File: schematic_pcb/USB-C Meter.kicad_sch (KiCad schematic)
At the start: 53 parts, among them J1 USB_B_Micro, J2 USB-C Receptacle 6P, J3 Generic IN, J4 Generic OUT, J5 USB-C Receptacle 6P, J6 Conn_Coaxial, J7 UART, U1 XL1509-3.3, U2 ME6211C33, U3 TPS2115, U4 ESP32-C3FH4, U6 INA228, U7 Display I2C, Y1 40MHz

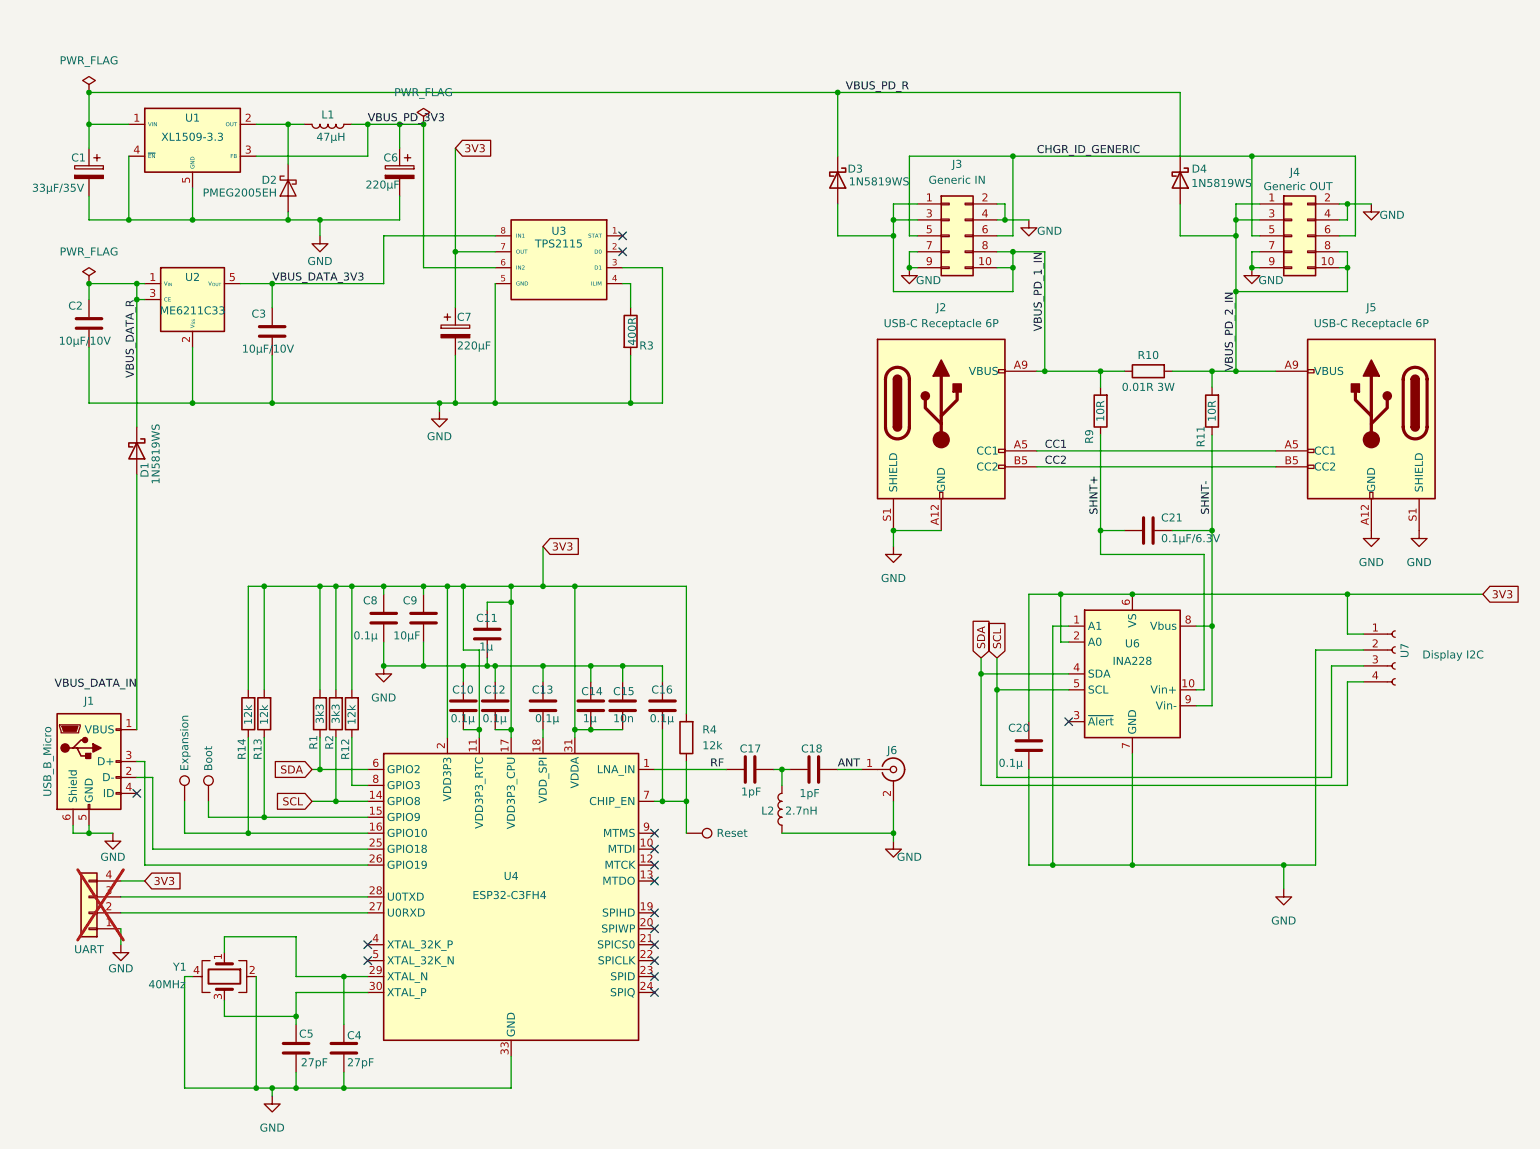
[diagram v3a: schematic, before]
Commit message: feat(hw): new buck converter enables up to 48V PD input
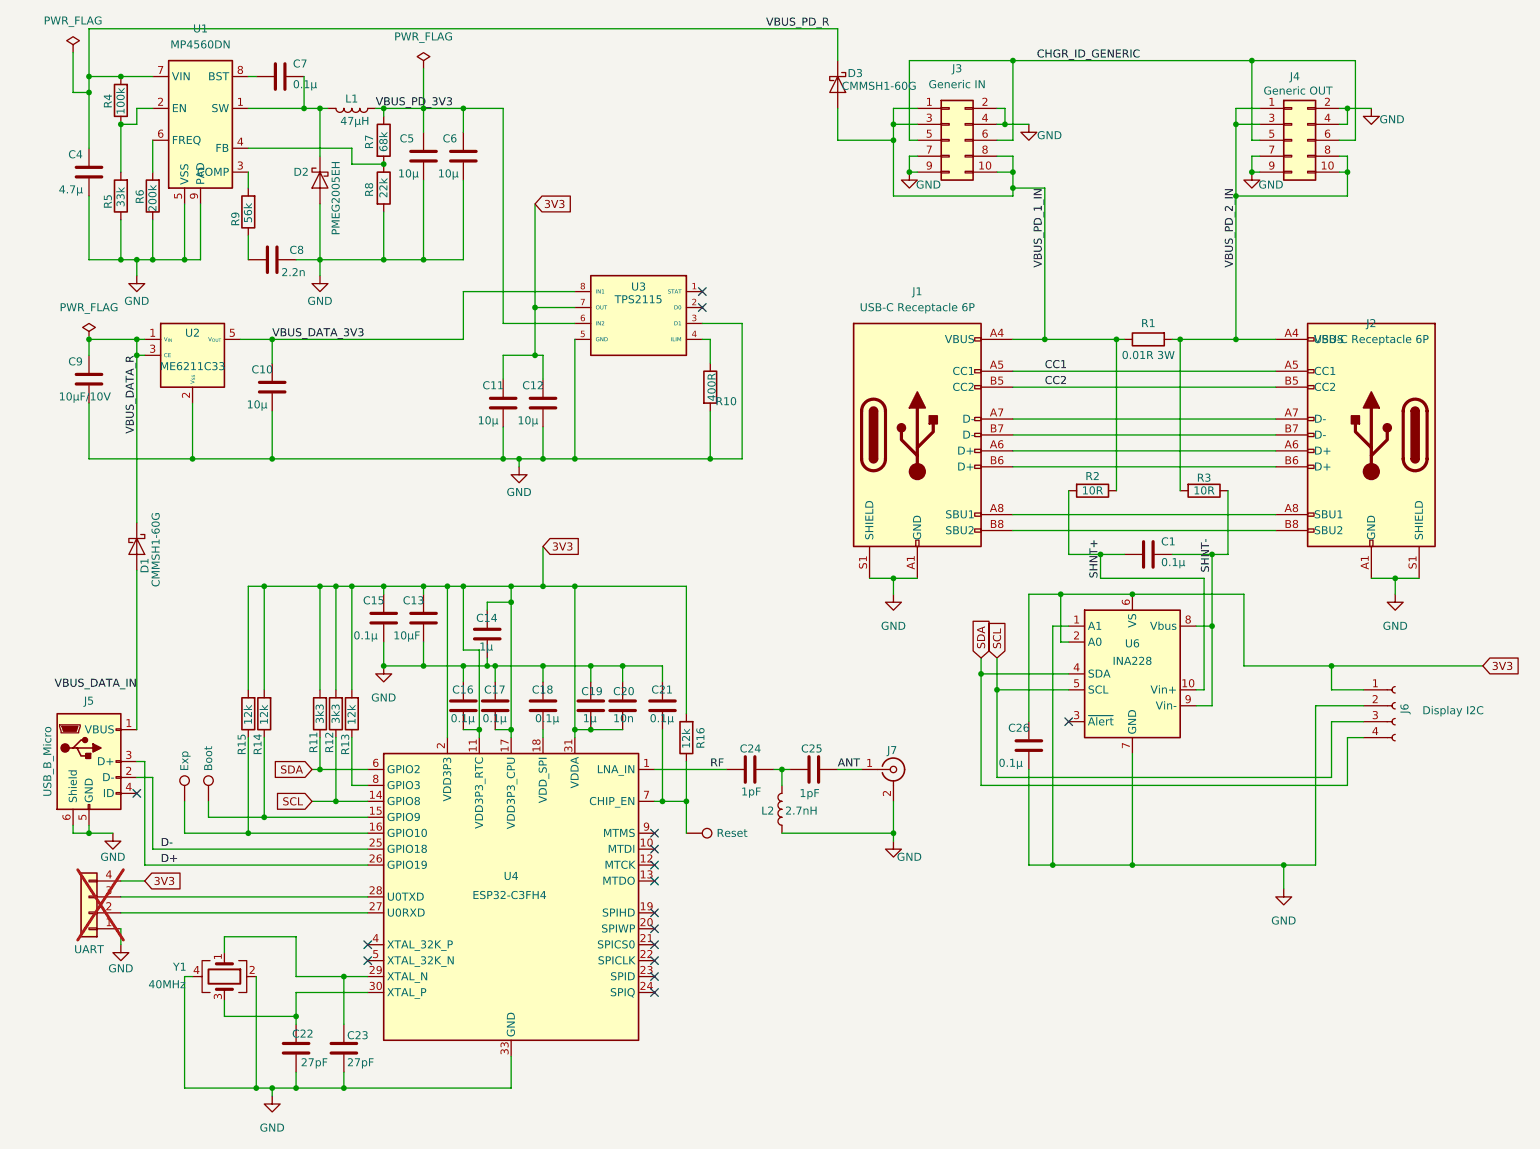
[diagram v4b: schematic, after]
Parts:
- removed C1: 33µF/35V, Capacitor_SMD:CP_Elec_5x5.8, symbol Device:C_Polarized
- removed C6, C7: 220µF, Capacitor_SMD:CP_Elec_6.3x5.9, symbol Device:C_Polarized
- removed D4: 1N5819WS, Diode_SMD:D_SOD-123F, symbol Diode:1N5819WS
- removed U1: XL1509-3.3, Package_SO:SOIC-8_3.9x4.9mm_P1.27mm, symbol Regulator_Switching:XL1509-3.3
- added C11, C12, C5, C6: 10µ, Capacitor_SMD:C_0603_1608Metric, symbol Device:C
- added C4: 4.7µ, Capacitor_SMD:C_0805_2012Metric_Pad1.18x1.45mm_HandSolder, symbol Device:C
- added C7: 0.1µ, Capacitor_SMD:C_0603_1608Metric, symbol Device:C
- added C8: 2.2n, Capacitor_SMD:C_0603_1608Metric, symbol Device:C
- added R4: 100k, Resistor_SMD:R_0603_1608Metric_Pad0.98x0.95mm_HandSolder, symbol Device:R
- added R5: 33k, Resistor_SMD:R_0603_1608Metric_Pad0.98x0.95mm_HandSolder, symbol Device:R
- added R6: 200k, Resistor_SMD:R_0603_1608Metric_Pad0.98x0.95mm_HandSolder, symbol Device:R
- added R7: 68k, Resistor_SMD:R_0603_1608Metric_Pad0.98x0.95mm_HandSolder, symbol Device:R
- added R8: 22k, Resistor_SMD:R_0603_1608Metric_Pad0.98x0.95mm_HandSolder, symbol Device:R
- added R9: 56k, Resistor_SMD:R_0603_1608Metric_Pad0.98x0.95mm_HandSolder, symbol Device:R
- added U1: MP4560DN, Package_SO:SOIC-8_3.9x4.9mm_P1.27mm, symbol Driver_FET:MP4560
- C1: renamed from C21; value 0.1µF/6.3V -> 0.1µ; Link (none) -> https://www.mouser.de/ProductDetail/YAGEO/CC0603MRY5V9BB104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; Price (none) -> 0,018
- C10: renamed from C3; value 10µF/10V -> 10µ; Link (none) -> https://www.mouser.de/ProductDetail/Samsung-Electro-Mechani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; Price (none) -> 0,20
- C13: renamed from C9; Link (none) -> https://www.mouser.de/ProductDetail/KYOCERA-AVX/06036D106MA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; Price (none) -> 0,058
- C14: renamed from C11; Link (none) -> https://www.mouser.de/ProductDetail/YAGEO/CC0603KRX5R8BB105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; Price (none) -> 0,034
- C15: renamed from C8; Link (none) -> https://www.mouser.de/ProductDetail/YAGEO/CC0603MRY5V9BB104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; Price (none) -> 0,018
- C16: renamed from C10; Link (none) -> https://www.mouser.de/ProductDetail/YAGEO/CC0603MRY5V9BB104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; Price (none) -> 0,018
- C17: renamed from C12; Link (none) -> https://www.mouser.de/ProductDetail/YAGEO/CC0603MRY5V9BB104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; Price (none) -> 0,018
- C18: renamed from C13; Link (none) -> https://www.mouser.de/ProductDetail/YAGEO/CC0603MRY5V9BB104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; Price (none) -> 0,018
- C19: renamed from C14; Link (none) -> https://www.mouser.de/ProductDetail/YAGEO/CC0603KRX5R8BB105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; Price (none) -> 0,034
- C20: renamed from C15; Link (none) -> https://www.mouser.de/ProductDetail/KYOCERA-AVX/06035C103K4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; Price (none) -> 0,074
- C21: renamed from C16; Link (none) -> https://www.mouser.de/ProductDetail/YAGEO/CC0603MRY5V9BB104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; Price (none) -> 0,018
- C22: renamed from C5; Link (none) -> https://www.mouser.de/ProductDetail/KYOCERA-AVX/04025A270JA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; Price (none) -> 0,016
- C23: renamed from C4; Link (none) -> https://www.mouser.de/ProductDetail/KYOCERA-AVX/04025A270JA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; Price (none) -> 0,016
- C24: renamed from C17; Link (none) -> https://www.mouser.de/ProductDetail/KYOCERA-AVX/04023A1R0BA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; Price (none) -> 0,163
- C25: renamed from C18; Link (none) -> https://www.mouser.de/ProductDetail/KYOCERA-AVX/04023A1R0BA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; Price (none) -> 0,163
- C26: renamed from C20; Link (none) -> https://www.mouser.de/ProductDetail/YAGEO/CC0603MRY5V9BB104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; Price (none) -> 0,018
- C9: renamed from C2; Link (none) -> https://www.mouser.de/ProductDetail/Samsung-Electro-Mechani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; Price (none) -> 0,20
- D1, D3: value 1N5819WS -> CMMSH1-60G; footprint Diode_SMD:D_SOD-123F -> Diode_SMD:Nexperia_CFP3_SOD-123W; symbol Diode:1N5819WS -> Diode:PMEG60T10ELR; Price (none) -> 0,218; url (none) -> https://www.mouser.de/ProductDetail/Nexperia/PMEG6010CEGW-Q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
- D2: Price (none) -> 0,092; url (none) -> https://www.mouser.de/ProductDetail/Nexperia/PMEG2005EH115?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
- J1: renamed from J2; footprint Connector_USB:USB_C_Receptacle_GCT_USB4125-xx-x_6P_TopMnt_Horizontal -> Connector_USB:USB_C_Receptacle_XKB_U262-16XN-4BVC11; symbol Connector:USB_C_Receptacle_PowerOnly_6P -> Connector:USB_C_Receptacle_USB2.0_16P
- J2: renamed from J5; footprint Connector_USB:USB_C_Receptacle_HRO_TYPE-C-31-M-17 -> Connector_USB:USB_C_Receptacle_XKB_U262-16XN-4BVC11; symbol Connector:USB_C_Receptacle_PowerOnly_6P -> Connector:USB_C_Receptacle_USB2.0_16P
- J3: Price (none) -> 0,791; url (none) -> https://www.mouser.de/ProductDetail/TE-Connectivity/826634-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
- J4: Price (none) -> 1,44; url (none) -> https://www.mouser.de/ProductDetail/Samtec/SSQ-105-02-T-D-R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
- J5: renamed from J1; Price (none) -> 1,74; url (none) -> https://www.mouser.de/ProductDetail/Wurth-Elektronik/629105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
- J6: renamed from U7; Price (none) -> 2,50; url (none) -> https://de.aliexpress.com/item/1005007759329196.html?spm=a2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
- J7: renamed from J6; Price (none) -> 1,12; url (none) -> https://www.mouser.de/ProductDetail/Hirose-Connector/U.FL-R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
- L1: Price (none) -> 1,05; url (none) -> https://www.mouser.de/ProductDetail/TE-Connectivity-Sigma-I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
- L2: Price (none) -> 0,123; url (none) -> https://www.mouser.de/ProductDetail/TE-Connectivity-Sigma-I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
- R1: renamed from R10; Price (none) -> 0,586; url (none) -> https://www.mouser.de/ProductDetail/Vishay-Dale/WSLP2512R01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
- R10: renamed from R3; Price (none) -> 0,086; url (none) -> https://www.mouser.de/ProductDetail/Vishay-Beyschlag/MCS040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
- R11: renamed from R1; Price (none) -> 0,086; url (none) -> https://www.mouser.de/ProductDetail/Bourns/CR0603-JW-332ELF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
- R12: renamed from R2; Price (none) -> 0,086; url (none) -> https://www.mouser.de/ProductDetail/Bourns/CR0603-JW-332ELF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
- R13: renamed from R12; Price (none) -> 0,086
- R14: renamed from R13; Price (none) -> 0,086
- R15: renamed from R14; Price (none) -> 0,086
- R16: renamed from R4; Price (none) -> 0,086
- R2: renamed from R9; Price (none) -> 0,086
- R3: renamed from R11; Price (none) -> 0,086
- TP1, TP3: now left out of the parts list
- TP2: value Expansion -> Exp; now left out of the parts list
- U2: Price (none) -> 0,50; url (none) -> https://www.mouser.de/ProductDetail/Microchip-Technology/MI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
- U3: Price (none) -> 1,69; url (none) -> https://www.mouser.de/ProductDetail/Texas-Instruments/TPS21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
- U4: Price (none) -> 1,81; url (none) -> https://www.mouser.de/ProductDetail/Espressif-Systems/ESP32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
- U6: Price (none) -> 2,97; url (none) -> https://www.mouser.de/ProductDetail/Texas-Instruments/INA22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
- Y1: Price (none) -> 0,367; url (none) -> https://www.mouser.de/ProductDetail/ECS/ECS-400-15-33B-CTN-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
- renumbered J7 to J8
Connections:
- net 3V3: now also C11.1, C12.1
- net GND: now also J1.A1 (GND), J1.B1 (GND), J2.A1 (GND), J2.B1 (GND), C11.2, C12.2, C4.2, C5.2, C6.2, C8.2, R5.1, R6.1, R8.2, U1.5 (VSS), U1.9 (PAD)
- net SHNT+: now also R2.2; no longer R2.1
- net SHNT-: no longer C1.2, R3.1, U6.8 (Vbus), U6.9 (Vin-)
- net VBUS_PD_1_IN: now also J1.A4 (VBUS), J1.B4 (VBUS), R2.1; no longer R2.2
- net VBUS_PD_2_IN: now also J2.A4 (VBUS), J2.B4 (VBUS)
- net VBUS_PD_3V3: now also C5.1, C6.1, R7.1
- net VBUS_PD_R: now also C4.1, R4.2, U1.7 (VIN)
- net D-: now reaches J5.2 (D-), U4.25 (GPIO18)
- net D+: now reaches J5.3 (D+), U4.26 (GPIO19)
- net at D2.1 (K), L1.1: now also C7.2, U1.1 (SW)
- new net: C1.2, R3.1, U6.8 (Vbus), U6.9 (Vin-)
- new net: R4.1, R5.2, U1.2 (EN)
- new net: R6.2, U1.6 (FREQ)
- new net: J1.A6 (D+), J2.A6 (D+)
- new net: J1.A7 (D-), J2.A7 (D-)
- new net: J1.A8 (SBU1), J2.A8 (SBU1)
- new net: J1.B6 (D+), J2.B6 (D+)
- new net: J1.B7 (D-), J2.B7 (D-)
- new net: J1.B8 (SBU2), J2.B8 (SBU2)
- new net: R7.2, R8.1, U1.4 (FB)
- new net: C8.1, R9.1
- new net: R9.2, U1.3 (COMP)
- new net: C7.1, U1.8 (BST)
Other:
- moved on the sheet: C1, C10, C9, D1, D2, D3, J3, J4, J6, L1, R1, R10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

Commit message: feat: schematic improvements (fix some component values)
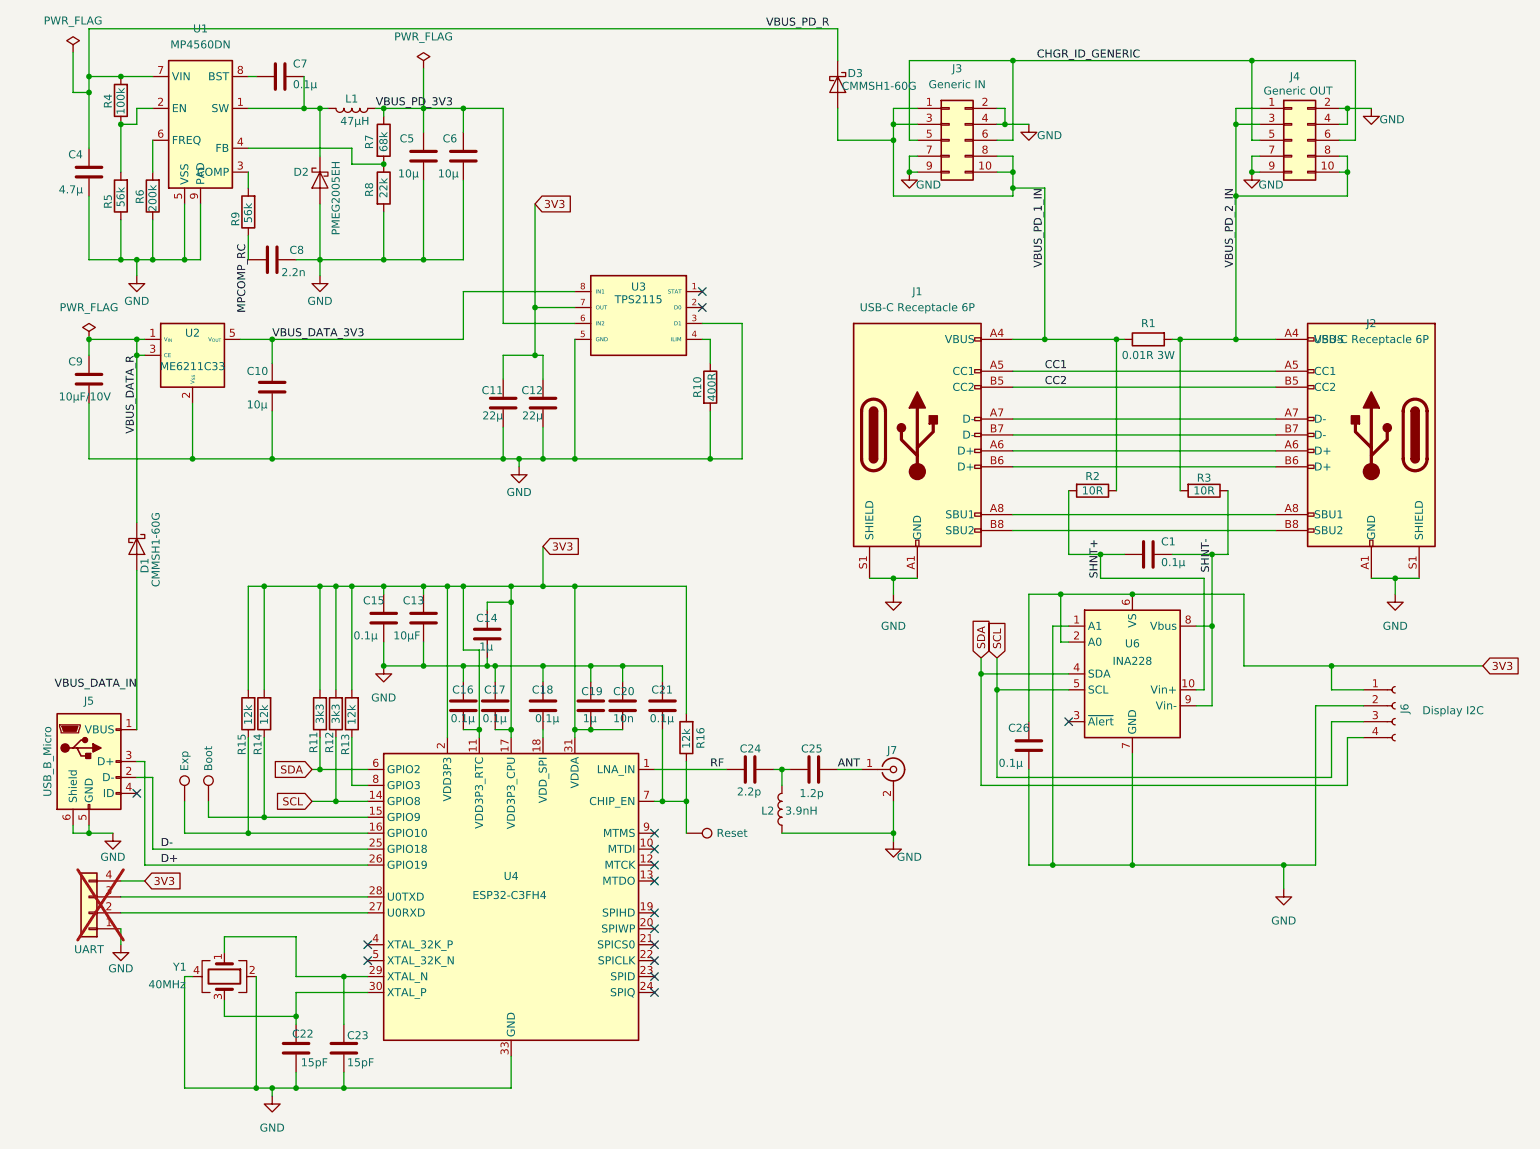
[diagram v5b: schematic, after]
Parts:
- C11, C12: value 10µ -> 22µ
- C22, C23: value 27pF -> 15pF
- C24: value 1pF -> 2.2p
- C25: value 1pF -> 1.2p
- L2: value 2.7nH -> 3.9nH
- R5: value 33k -> 56k
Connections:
- net MPCOMP_RC: now reaches C8.1, R9.1
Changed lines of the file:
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@@
 	(wire
 		(pts
-			(xy 46.99 53.34) (xy 46.99 49.53)
-		)
-		(stroke
-			(width 0)
-			(type default)
-		)
-	)
-	(wire
-		(pts
 			(xy 54.61 167.64) (xy 62.23 167.64)
 		)
@@
 	(wire
 		(pts
+			(xy 46.99 49.53) (xy 46.99 53.34)
+		)
+		(stroke
+			(width 0)
+			(type default)
+		)
+	)
+	(wire
+		(pts
 			(xy 195.58 66.04) (xy 204.47 66.04)
 		)
@@
 		)
 	)
+	(label "MPCOMP_RC"
+		(at 46.99 50.8 270)
+		(effects
+			(font
+				(size 1.27 1.27)
+			)
+			(justify right bottom)
+		)
+	)
 	(label "SHNT+"
 		(at 182.88 104.14 90)
@@
 			)
 		)
-		(property "Value" "33k"
+		(property "Value" "56k"
 			(at 26.67 44.958 90)
 			(effects
@@
 			)
 		)
-		(property "Value" "27pF"
+		(property "Value" "15pF"
 			(at 62.738 181.356 0)
 			(effects
@@
 			)
 		)
-		(property "Value" "1pF"
+		(property "Value" "1.2p"
 			(at 134.874 138.43 90)
 			(effects
@@
 		(dnp no)
 		(property "Reference" "C12"
-			(at 90.678 73.406 0)
+			(at 93.98 74.93 0)
 			(effects
 				(font
 					(size 1.27 1.27)
 				)
-				(justify left)
+				(justify right bottom)
 			)
 		)
-		(property "Value" "10µ"
-			(at 89.916 78.994 0)
+		(property "Value" "22µ"
+			(at 93.98 77.47 0)
 			(effects
 				(font
 					(size 1.27 1.27)
 				)
-				(justify left)
+				(justify right top)
 			)
 		)
@@
 			)
 		)
-		(property "Value" "2.7nH"
+		(property "Value" "3.9nH"
 			(at 132.588 141.224 0)
 			(effects
@@
 			)
 		)
-		(property "Value" "1pF"
+		(property "Value" "2.2p"
 			(at 128.778 138.176 90)
 			(effects
@@
 		(dnp no)
 		(property "Reference" "C11"
-			(at 84.328 73.406 0)
+			(at 87.63 74.93 0)
 			(effects
 				(font
 					(size 1.27 1.27)
 				)
-				(justify left)
+				(justify right bottom)
 			)
 		)
-		(property "Value" "10µ"
-			(at 83.566 78.994 0)
+		(property "Value" "22µ"
+			(at 87.63 77.47 0)
 			(effects
 				(font
 					(size 1.27 1.27)
 				)
-				(justify left)
+				(justify right top)
 			)
 		)
@@
 			)
 		)
-		(property "Value" "27pF"
+		(property "Value" "15pF"
 			(at 59.69 181.356 0)
 			(effects
@@
 		(dnp no)
 		(property "Reference" "C10"
-			(at 47.498 70.866 0)
+			(at 46.736 71.12 0)
 			(effects
 				(font
@@
 		(dnp no)
 		(property "Reference" "R10"
-			(at 123.19 75.946 0)
+			(at 118.618 73.66 90)
 			(effects
 				(font

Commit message: fix: schematic/pcb v2.4 (wip)
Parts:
- removed C14: 1µ, Capacitor_SMD:C_0603_1608Metric, symbol Device:C
- removed J8: UART, Connector_PinHeader_1.00mm:PinHeader_1x04_P1.00mm_Vertical_SMD_Pin1Left, symbol Connector_Generic:Conn_01x04
- added C2: 10µ, Capacitor_SMD:C_0603_1608Metric, symbol Device:C
- added C27, C28: .1µ, Capacitor_SMD:C_0603_1608Metric, symbol Device:C
- added C29: 1µ, Capacitor_SMD:C_0603_1608Metric, symbol Device:C
- added C3: 0.1µ, Capacitor_SMD:C_0603_1608Metric, symbol Device:C
- added TP4: TXD, TestPoint:TestPoint_Pad_D1.5mm, symbol Connector:TestPoint
- added TP5: RXD, TestPoint:TestPoint_Pad_D1.5mm, symbol Connector:TestPoint
- added TP6: GND, TestPoint:TestPoint_Pad_D1.5mm, symbol Connector:TestPoint
- C12: value 22µ -> 47µ; footprint Capacitor_SMD:C_0603_1608Metric -> Capacitor_Tantalum_SMD:CP_EIA-3528-12_Kemet-T_HandSolder; symbol Device:C -> Device:C_Polarized
- C20: value 10n -> .1µ
- C4: value 4.7µ -> 10µ
- C9: value 10µF/10V -> 10µ
- D1, D3: value CMMSH1-60G -> DS60_1
- J1, J2: value USB-C Receptacle 6P -> USB-C Receptacle 16P
- R14, R15: value 12k -> 10k
- R2, R3: footprint Resistor_SMD:R_0402_1005Metric -> Resistor_SMD:R_0603_1608Metric_Pad0.98x0.95mm_HandSolder
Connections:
- net 3V3: now also C2.1, C27.1
- net GND: now also C2.2, C27.2, C28.2, C29.2, C3.2, TP6.1
- net VBUS_DATA_3V3: now also C28.1, C29.1
- net at C1.2, R3.1, U6.8 (Vbus)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: now also C3.1
- net at U4.27 (U0RXD): now also TP5.1
- net at U4.28 (U0TXD): now also TP4.1
- net CHGR_ID_GENERIC renamed CHGR_ID_GENERIC_A
- net CHGR_ID_GENERIC_A: no longer J3.6 (Pin_6), J4.6 (Pin_6)
- new net CHGR_ID_GENERIC_B: J3.6 (Pin_6), J4.6 (Pin_6)
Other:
- moved on the sheet: C11
